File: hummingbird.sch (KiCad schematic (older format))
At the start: 42 parts, among them J1 JST, J2 ANEMOMETER, J3 USB_B_Micro, J4 Expansion, J5 SWD_PROG, J6 microSD, J7 SOIC_CLIP, J8 Antenna, SW1 SW_DPDT_x2, U1 MCP73831-2-OT, U2 AP2112K-3.3, U3 W25Q64JVSSIM, U4 ATSAMD21G18A-AUT, U5 RFM95W-915S2, U6 BMP388, Y1 32.768 Hz

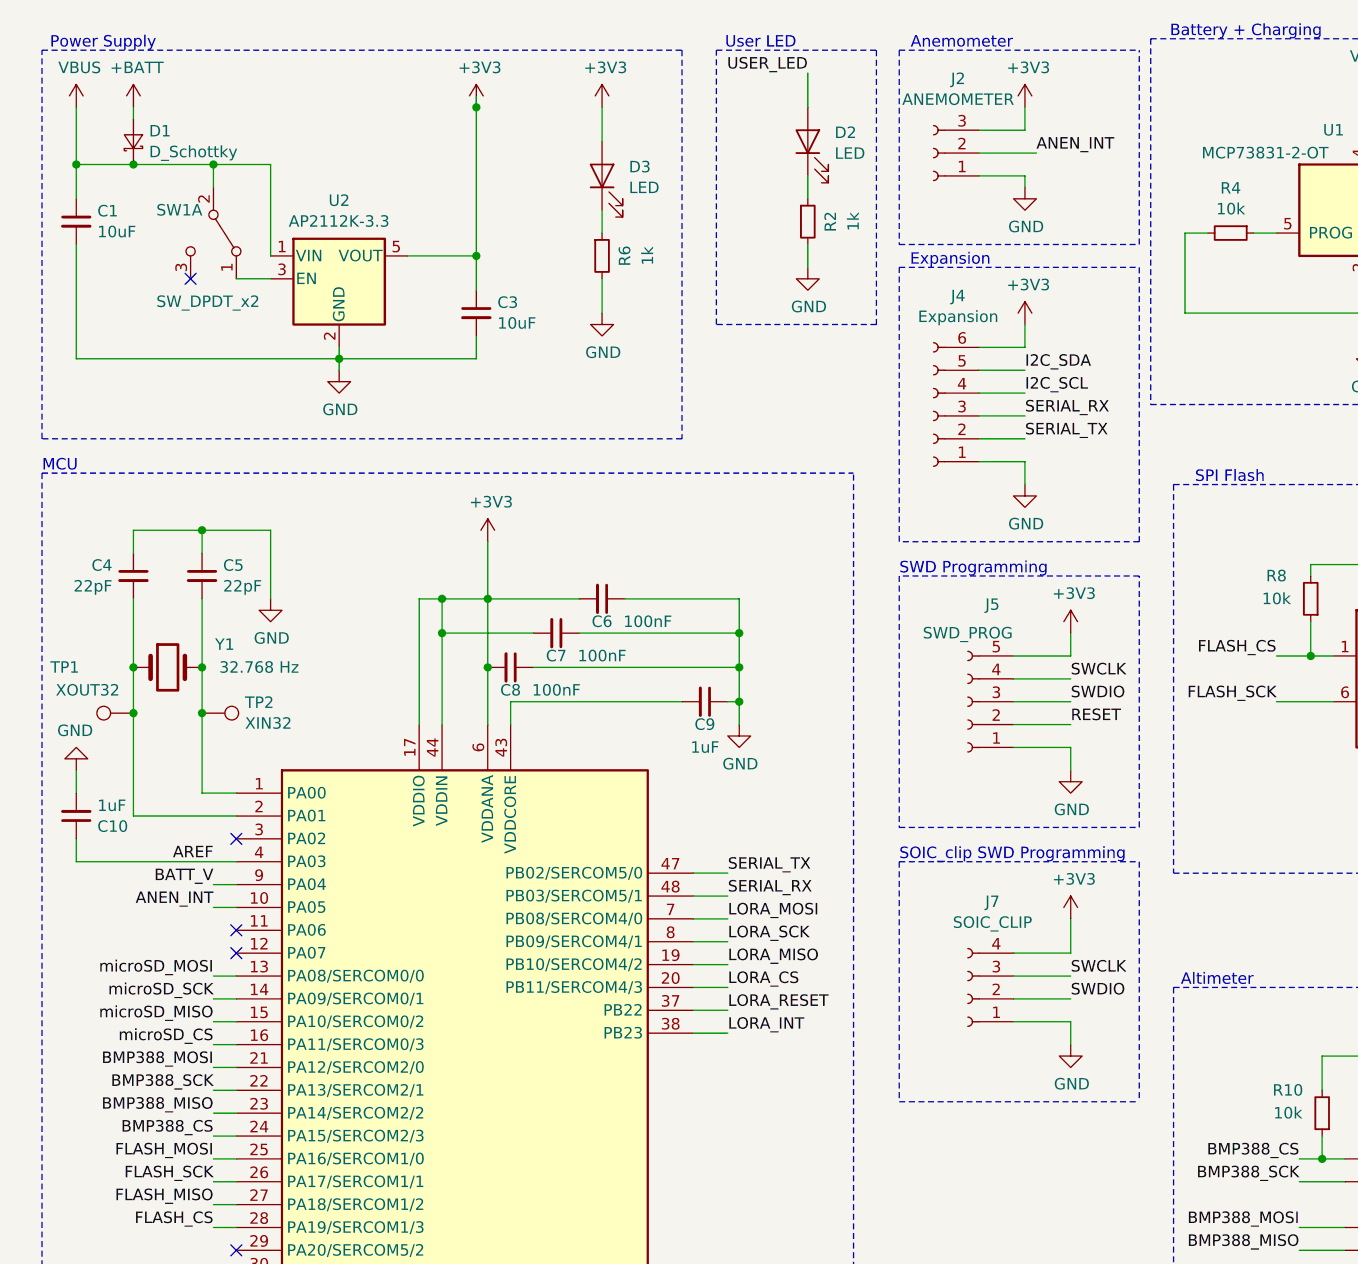
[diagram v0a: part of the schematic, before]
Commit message: remove SOICbyte, start layout over, rejigger pinouts
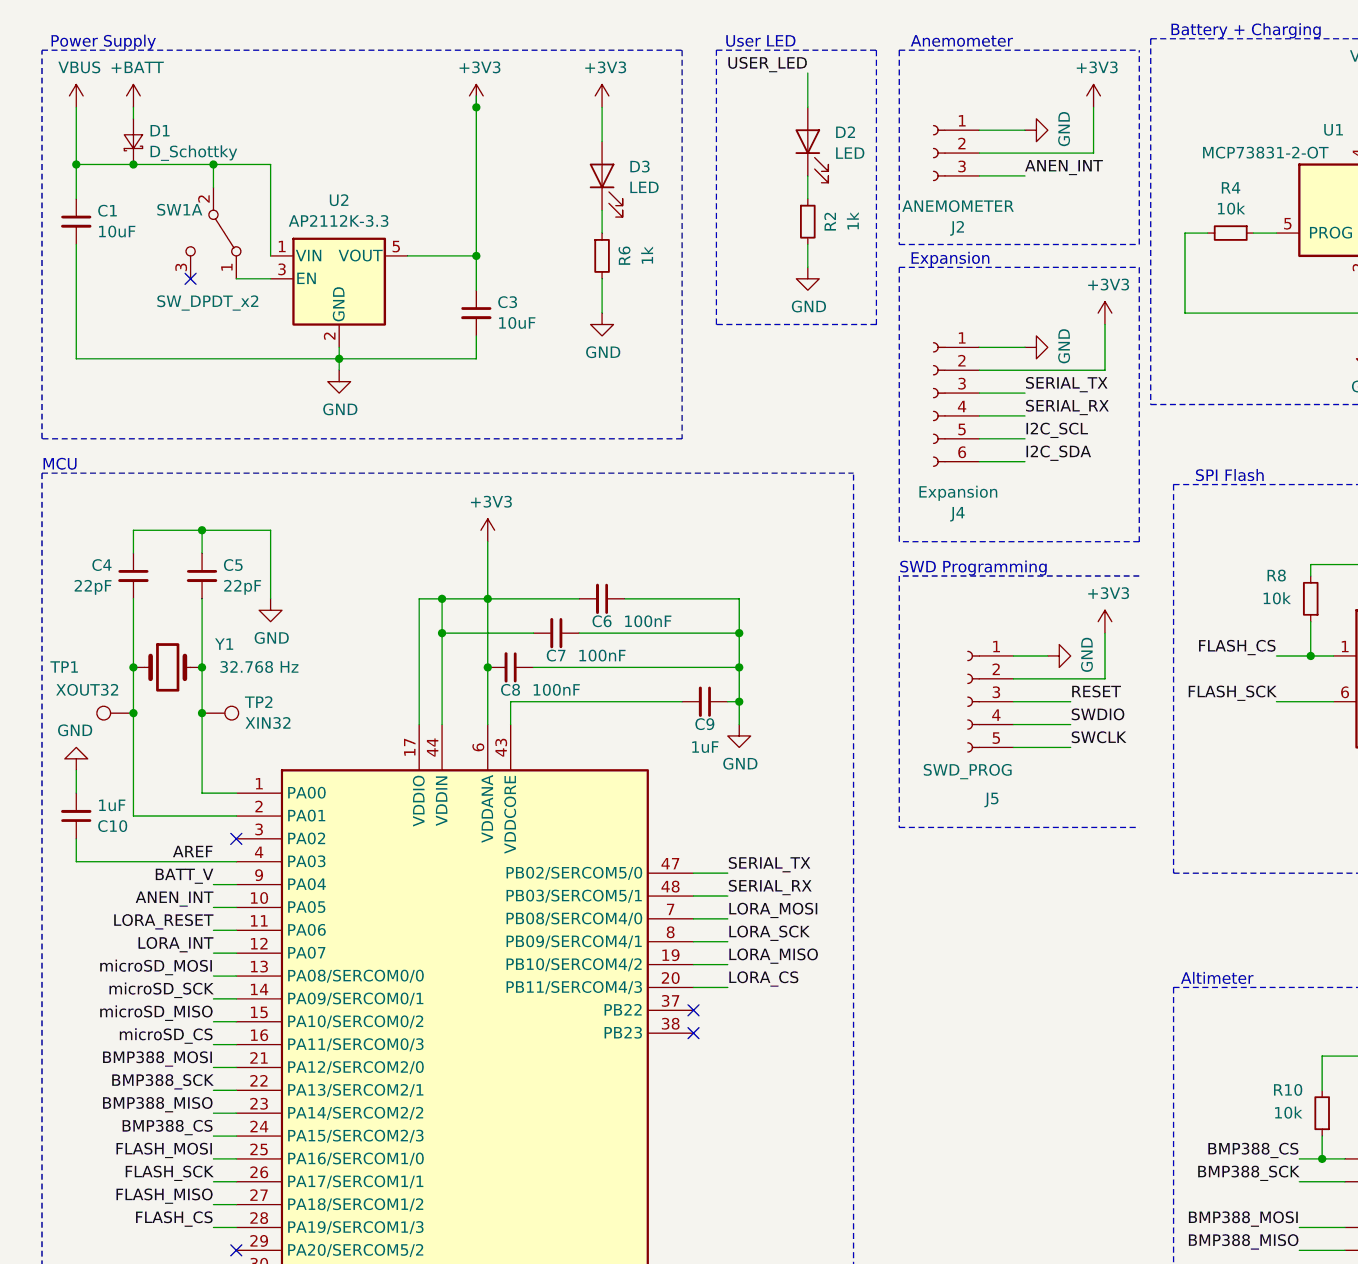
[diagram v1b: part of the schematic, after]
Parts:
- removed J7: SOIC_CLIP, footprints:SOIC_clipProgSmall, symbol Connector:Conn_01x04_Female
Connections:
- net +3V3: now also J2.2 (Pin_2), J4.2 (Pin_2), J5.2 (Pin_2); no longer J2.3 (Pin_3), J4.6 (Pin_6), J5.5 (Pin_5)
- net ANEN_INT: now also J2.3 (Pin_3); no longer J2.2 (Pin_2)
- net I2C_SCL: now also J4.5 (Pin_5); no longer J4.4 (Pin_4)
- net I2C_SDA: now also J4.6 (Pin_6); no longer J4.5 (Pin_5)
- net LORA_INT: now also U4.12 (PA07); no longer U4.38 (PB23)
- net LORA_RESET: now also U4.11 (PA06); no longer U4.37 (PB22)
- net RESET: now also J5.3 (Pin_3); no longer J5.2 (Pin_2)
- net SERIAL_RX: now also J4.4 (Pin_4); no longer J4.3 (Pin_3)
- net SERIAL_TX: now also J4.3 (Pin_3); no longer J4.2 (Pin_2)
- net SWCLK: now also J5.5 (Pin_5); no longer J5.4 (Pin_4)
- net SWDIO: now also J5.4 (Pin_4); no longer J5.3 (Pin_3)
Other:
- note removed: "SOIC_clip SWD Programming"
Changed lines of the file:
@@
 F 4 "~" H 4650 3500 50  0001 C CNN "DigiKey Part Number"
 	1    4650 3500
-	-1   0    0    1
+	-1   0    0    -1
 $EndComp
 Wire Wire Line
@@
 L power:GND #PWR0129
 U 1 1 5D16B7BA
-P 5100 3800
-F 0 "#PWR0129" H 5100 3550 50  0001 C CNN
-F 1 "GND" H 5105 3627 50  0000 C CNN
-F 2 "" H 5100 3800 50  0001 C CNN
-F 3 "" H 5100 3800 50  0001 C CNN
-	1    5100 3800
-	1    0    0    -1
-$EndComp
-Wire Wire Line
-	5100 3700 5100 3800
-Wire Wire Line
-	4850 3300 5100 3300
-Wire Wire Line
-	5100 3300 5100 3200
+P 5000 3300
+F 0 "#PWR0129" H 5000 3050 50  0001 C CNN
+F 1 "GND" H 5005 3127 50  0000 C CNN
+F 2 "" H 5000 3300 50  0001 C CNN
+F 3 "" H 5000 3300 50  0001 C CNN
+	1    5000 3300
+	0    -1   -1   0
+$EndComp
 $Comp
 L power:+3V3 #PWR0130
 U 1 1 5D1782FB
-P 5100 3200
-F 0 "#PWR0130" H 5100 3050 50  0001 C CNN
-F 1 "+3V3" H 5115 3373 50  0000 C CNN
-F 2 "" H 5100 3200 50  0001 C CNN
-F 3 "" H 5100 3200 50  0001 C CNN
-	1    5100 3200
+P 5250 3200
+F 0 "#PWR0130" H 5250 3050 50  0001 C CNN
+F 1 "+3V3" H 5265 3373 50  0000 C CNN
+F 2 "" H 5250 3200 50  0001 C CNN
+F 3 "" H 5250 3200 50  0001 C CNN
+	1    5250 3200
 	1    0    0    -1
 $EndComp
 Wire Wire Line
-	4850 3400 5100 3400
-Wire Wire Line
 	4850 3500 5100 3500
 Wire Wire Line
 	4850 3600 5100 3600
-Text Label 5100 3400 0    50   ~ 0
+Text Label 5100 3700 0    50   ~ 0
 SWCLK
+Text Label 5100 3600 0    50   ~ 0
+SWDIO
 Text Label 5100 3500 0    50   ~ 0
-SWDIO
-Text Label 5100 3600 0    50   ~ 0
 RESET
 Text Label 1350 6500 2    50   ~ 0
@@
 Text Label 3600 4750 0    50   ~ 0
 LORA_CS
-Text Label 3600 4850 0    50   ~ 0
+Text Label 1350 4500 2    50   ~ 0
 LORA_RESET
-Text Label 3600 4950 0    50   ~ 0
+Text Label 1350 4600 2    50   ~ 0
 LORA_INT
 Wire Wire Line
@@
 Wire Wire Line
 	3450 4750 3600 4750
-Wire Wire Line
-	3450 4850 3600 4850
-Wire Wire Line
-	3450 4950 3600 4950
 Wire Wire Line
 	7250 3200 7350 3200
@@
 F 4 "~" H 4500 1100 50  0001 C CNN "DigiKey Part Number"
 	1    4500 1100
-	-1   0    0    1
+	-1   0    0    -1
 $EndComp
 $Comp
 L Connector:Conn_01x06_Female J4
 U 1 1 5D154284
-P 4500 2250
-F 0 "J4" H 4392 1725 50  0000 C CNN
-F 1 "Expansion" H 4392 1816 50  0000 C CNN
-F 2 "footprints:PinSocket_1x06_P2.54mm_Vertical" H 4500 2250 50  0001 C CNN
-F 3 "~" H 4500 2250 50  0001 C CNN
-F 4 "~" H 4500 2250 50  0001 C CNN "DigiKey Part Number"
-	1    4500 2250
-	-1   0    0    1
+P 4500 2150
+F 0 "J4" H 4392 1625 50  0000 C CNN
+F 1 "Expansion" H 4392 1716 50  0000 C CNN
+F 2 "footprints:PinSocket_1x06_P2.54mm_Vertical" H 4500 2150 50  0001 C CNN
+F 3 "~" H 4500 2150 50  0001 C CNN
+F 4 "~" H 4500 2150 50  0001 C CNN "DigiKey Part Number"
+	1    4500 2150
+	-1   0    0    -1
 $EndComp
 $Comp
 L power:+3V3 #PWR0132
 U 1 1 5D154BAD
-P 4900 900
-F 0 "#PWR0132" H 4900 750 50  0001 C CNN
-F 1 "+3V3" H 4915 1073 50  0000 C CNN
-F 2 "" H 4900 900 50  0001 C CNN
-F 3 "" H 4900 900 50  0001 C CNN
-	1    4900 900
+P 5200 900
+F 0 "#PWR0132" H 5200 750 50  0001 C CNN
+F 1 "+3V3" H 5215 1073 50  0000 C CNN
+F 2 "" H 5200 900 50  0001 C CNN
+F 3 "" H 5200 900 50  0001 C CNN
+	1    5200 900
 	1    0    0    -1
 $EndComp
@@
 L power:GND #PWR0133
 U 1 1 5D1699C3
-P 4900 1250
-F 0 "#PWR0133" H 4900 1000 50  0001 C CNN
-F 1 "GND" H 4905 1077 50  0000 C CNN
-F 2 "" H 4900 1250 50  0001 C CNN
-F 3 "" H 4900 1250 50  0001 C CNN
-	1    4900 1250
-	1    0    0    -1
-$EndComp
-Text Label 4950 1100 0    50   ~ 0
+P 4900 1000
+F 0 "#PWR0133" H 4900 750 50  0001 C CNN
+F 1 "GND" H 4905 827 50  0000 C CNN
+F 2 "" H 4900 1000 50  0001 C CNN
+F 3 "" H 4900 1000 50  0001 C CNN
+	1    4900 1000
+	0    -1   -1   0
+$EndComp
+Text Label 4900 1200 0    50   ~ 0
 ANEN_INT
-Wire Wire Line
-	4700 1100 4950 1100
 $Comp
 L power:GND #PWR0134
 U 1 1 5D1A8337
-P 4900 2550
-F 0 "#PWR0134" H 4900 2300 50  0001 C CNN
-F 1 "GND" H 4905 2377 50  0000 C CNN
-F 2 "" H 4900 2550 50  0001 C CNN
-F 3 "" H 4900 2550 50  0001 C CNN
-	1    4900 2550
-	1    0    0    -1
+P 4900 1950
+F 0 "#PWR0134" H 4900 1700 50  0001 C CNN
+F 1 "GND" H 4905 1777 50  0000 C CNN
+F 2 "" H 4900 1950 50  0001 C CNN
+F 3 "" H 4900 1950 50  0001 C CNN
+	1    4900 1950
+	0    -1   -1   0
 $EndComp
 Wire Wire Line
 	4700 2450 4900 2450
-Wire Wire Line
-	4900 2450 4900 2550
 $Comp
 L power:+3V3 #PWR0135
 U 1 1 5D1B30B8
-P 4900 1850
-F 0 "#PWR0135" H 4900 1700 50  0001 C CNN
-F 1 "+3V3" H 4915 2023 50  0000 C CNN
-F 2 "" H 4900 1850 50  0001 C CNN
-F 3 "" H 4900 1850 50  0001 C CNN
-	1    4900 1850
+P 5250 1850
+F 0 "#PWR0135" H 5250 1700 50  0001 C CNN
+F 1 "+3V3" H 5265 2023 50  0000 C CNN
+F 2 "" H 5250 1850 50  0001 C CNN
+F 3 "" H 5250 1850 50  0001 C CNN
+	1    5250 1850
 	1    0    0    -1
 $EndComp
 Wire Wire Line
 	4700 1950 4900 1950
-Wire Wire Line
-	4900 1950 4900 1850
-Wire Wire Line
-	4700 2050 4900 2050
-Text Label 4900 2050 0    50   ~ 0
+Text Label 4900 2450 0    50   ~ 0
 I2C_SDA
 Wire Wire Line
 	4700 2150 4900 2150
-Text Label 4900 2150 0    50   ~ 0
+Text Label 4900 2350 0    50   ~ 0
 I2C_SCL
 Wire Wire Line
@@
 Wire Wire Line
 	4700 2350 4900 2350
-Text Label 4900 2350 0    50   ~ 0
+Text Label 4900 2150 0    50   ~ 0
 SERIAL_TX
 Text Label 1350 5800 2    50   ~ 0
@@
 	4350 4050 5400 4050
 Wire Notes Line
-	5400 4050 5400 2950
-Wire Notes Line
 	5400 2950 4350 2950
 Wire Notes Line
@@
 Text Notes 4350 2950 0    50   ~ 0
 SWD Programming
-$Comp
-L Connector:Conn_01x04_Female J7
-U 1 1 5D4418E8
-P 4650 4800
-F 0 "J7" H 4542 4375 50  0000 C CNN
-F 1 "SOIC_CLIP" H 4542 4466 50  0000 C CNN
-F 2 "footprints:SOIC_clipProgSmall" H 4650 4800 50  0001 C CNN
-F 3 "https://hackaday.io/project/165917-soicbite-programmingdebug-connector-footprint" H 4650 4800 50  0001 C CNN
-F 4 "~" H 4650 4800 50  0000 C CNN "DigiKey Part Number"
-	1    4650 4800
-	-1   0    0    1
-$EndComp
-$Comp
-L power:+3V3 #PWR0136
-U 1 1 5D46ECBA
-P 5100 4450
-F 0 "#PWR0136" H 5100 4300 50  0001 C CNN
-F 1 "+3V3" H 5115 4623 50  0000 C CNN
-F 2 "" H 5100 4450 50  0001 C CNN
-F 3 "" H 5100 4450 50  0001 C CNN
-	1    5100 4450
-	1    0    0    -1
-$EndComp
-Wire Wire Line
-	5100 4450 5100 4600
-Wire Wire Line
-	5100 4600 4850 4600
-Text Label 5100 4700 0    50   ~ 0
-SWCLK
-Text Label 5100 4800 0    50   ~ 0
-SWDIO
-$Comp
-L power:GND #PWR0137
-U 1 1 5D47DC25
-P 5100 5000
-F 0 "#PWR0137" H 5100 4750 50  0001 C CNN
-F 1 "GND" H 5105 4827 50  0000 C CNN
-F 2 "" H 5100 5000 50  0001 C CNN
-F 3 "" H 5100 5000 50  0001 C CNN
-	1    5100 5000
-	1    0    0    -1
-$EndComp
-Wire Wire Line
-	4850 4900 5100 4900
-Wire Wire Line
-	5100 4900 5100 5000
-Text Notes 4350 4200 0    50   ~ 0
-SOIC_clip SWD Programming
-Wire Wire Line
-	4850 4800 5100 4800
-Wire Wire Line
-	4850 4700 5100 4700
-Wire Notes Line
-	4350 5250 5400 5250
-Wire Notes Line
-	4350 4200 4350 5250
-Wire Notes Line
-	5400 4200 5400 5250
-Wire Notes Line
-	4350 4200 5400 4200
-NoConn ~ 1450 4500
-NoConn ~ 1450 4600
 NoConn ~ 1450 5900
 NoConn ~ 1450 6000
@@
 Wire Wire Line
 	4700 1200 4900 1200
-Wire Wire Line
-	4900 1200 4900 1250
-Wire Wire Line
-	4900 900  4900 1000
 Wire Wire Line
 	4900 1000 4700 1000
@@
 Wire Wire Line
 	9600 5350 9900 5350
+NoConn ~ 3450 4850
+NoConn ~ 3450 4950
+Wire Wire Line
+	1350 4500 1450 4500
+Wire Wire Line
+	1450 4600 1350 4600
+Wire Wire Line
+	5250 3400 5250 3200
+Wire Wire Line
+	4850 3400 5250 3400
+Wire Wire Line
+	4850 3300 5000 3300
+Wire Wire Line
+	5250 2050 5250 1850
+Wire Wire Line
+	4700 2050 5250 2050
+Wire Wire Line
+	5200 1100 5200 900
+Wire Wire Line
+	4700 1100 5200 1100
 $EndSCHEMATC
